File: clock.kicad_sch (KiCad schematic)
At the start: 8 parts, among them U17 74HC74, U9 74HCU04, Y1 3.58Mhz

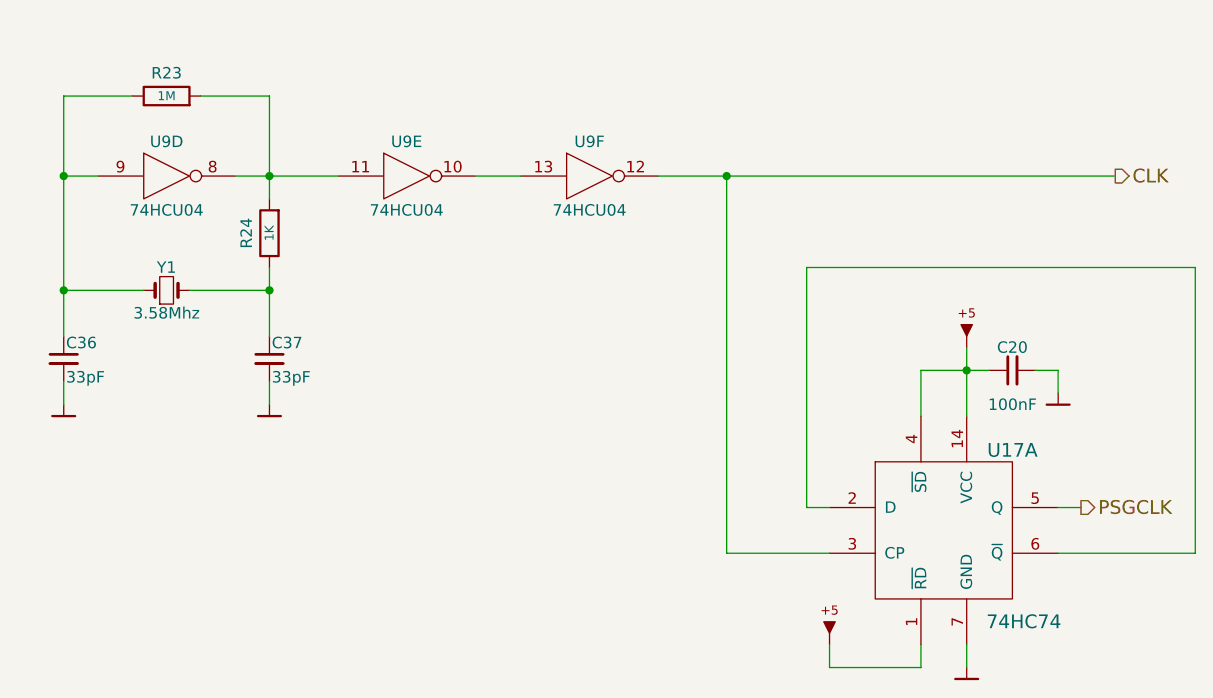
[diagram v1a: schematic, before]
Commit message: Use clock generator IC instead of oscillator
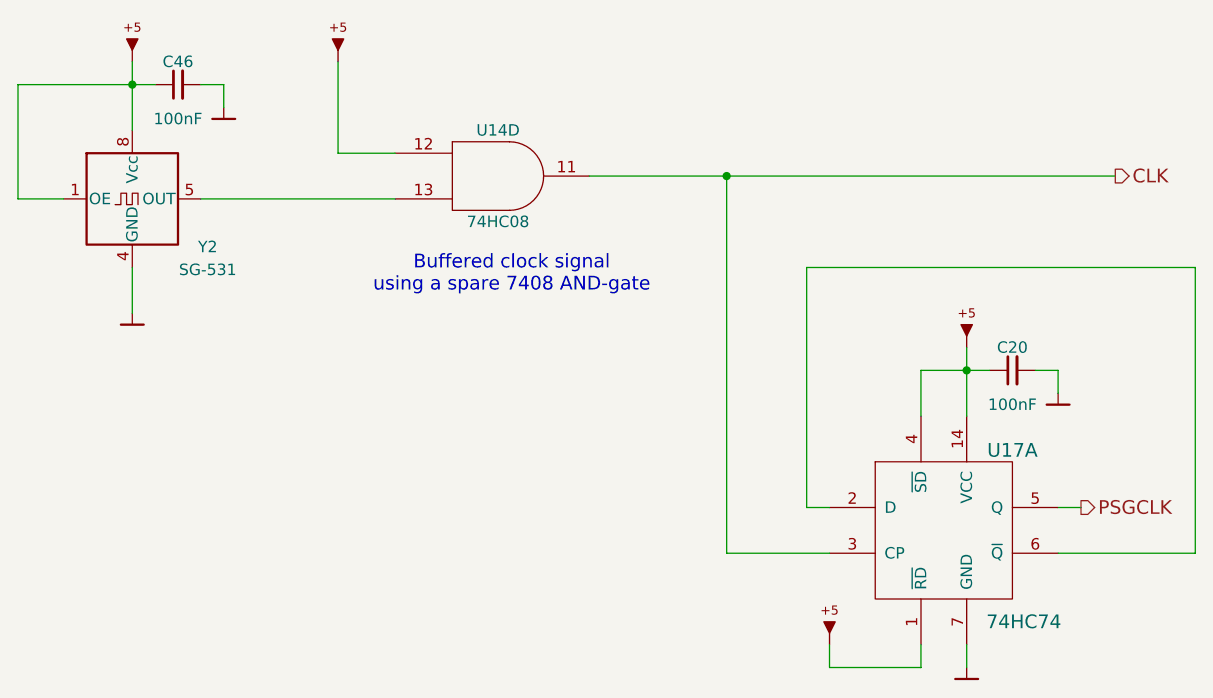
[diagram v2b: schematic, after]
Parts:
- removed C36, C37: 33pF, PCM_artemisa:Disc_capacitor, symbol PCM_artemisa:Cap
- removed R23: 1M, PCM_artemisa:Axial_resistor, symbol PCM_artemisa:R
- removed R24: 1K, PCM_artemisa:Axial_resistor, symbol PCM_artemisa:R
- removed U9: 74HCU04, PCM_artemisa:DIP-14_300, symbol PCM_artemisa:74HCU04
- removed Y1: 3.58Mhz, PCM_artemisa:Crystal, symbol PCM_artemisa:Crystal
- added C46: 100nF, PCM_artemisa:Disc_capacitor, symbol PCM_artemisa:Cap
- added U14: 74HC08, PCM_artemisa:DIP-14_300, symbol PCM_artemisa:74HC08
- added Y2: SG-531, Oscillator:Oscillator_SeikoEpson_SG-8002DC, symbol PCM_artemisa:SG-531
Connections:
- net CLK: now also U14.11
- net GND: now also C46.2, Y2.4 (GND)
- net VCC: now also C46.1, U14.12, Y2.1 (OE), Y2.8 (Vcc)
- new net: U14.13, Y2.5 (OUT)
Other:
- note added: "Buffered clock signal using a spare 7408 AND-gate"

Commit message: Re-annotate the whole schematic
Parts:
- renumbered C46 to C19, U14 to U6, U17 to U8, Y2 to Y1
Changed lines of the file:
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@@
 		(in_pos_files yes)
 		(dnp no)
-		(property "Reference" "U17"
+		(property "Reference" "U8"
 			(at 179.07 105.41 0)
 			(show_name no)
@@
 			(project "motherboard-hk10"
 				(path "/e63e39d7-6ac0-4ffd-8aa3-1841a4541b55/00000000-0000-0000-0000-00005bf74a85"
-					(reference "U17")
+					(reference "U8")
 					(unit 1)
 				)
@@
 		(in_pos_files yes)
 		(dnp no)
-		(property "Reference" "#PWR0127"
+		(property "Reference" "#PWR073"
 			(at 173.99 95.25 0)
 			(hide yes)
@@
 			(project "motherboard-hk10"
 				(path "/e63e39d7-6ac0-4ffd-8aa3-1841a4541b55/00000000-0000-0000-0000-00005bf74a85"
-					(reference "#PWR0127")
+					(reference "#PWR073")
 					(unit 1)
 				)
@@
 		(in_pos_files yes)
 		(dnp no)
-		(property "Reference" "#PWR0130"
+		(property "Reference" "#PWR072"
 			(at 158.75 128.27 0)
 			(hide yes)
@@
 			(project "motherboard-hk10"
 				(path "/e63e39d7-6ac0-4ffd-8aa3-1841a4541b55/00000000-0000-0000-0000-00005bf74a85"
-					(reference "#PWR0130")
+					(reference "#PWR072")
 					(unit 1)
 				)
@@
 		(in_pos_files yes)
 		(dnp no)
-		(property "Reference" "#PWR0163"
+		(property "Reference" "#PWR075"
 			(at 184.15 101.6 0)
 			(hide yes)
@@
 			(project "motherboard-hk10"
 				(path "/e63e39d7-6ac0-4ffd-8aa3-1841a4541b55/00000000-0000-0000-0000-00005bf74a85"
-					(reference "#PWR0163")
+					(reference "#PWR075")
 					(unit 1)
 				)
@@
 		(in_pos_files yes)
 		(dnp no)
-		(property "Reference" "#PWR0179"
+		(property "Reference" "#PWR074"
 			(at 173.99 132.08 0)
 			(hide yes)
@@
 			(project "motherboard-hk10"
 				(path "/e63e39d7-6ac0-4ffd-8aa3-1841a4541b55/00000000-0000-0000-0000-00005bf74a85"
-					(reference "#PWR0179")
+					(reference "#PWR074")
 					(unit 1)
 				)
@@
 		(in_pos_files yes)
 		(dnp no)
-		(property "Reference" "Y2"
+		(property "Reference" "Y1"
 			(at 89.662 82.804 0)
 			(show_name no)
@@
 			(project "motherboard-hk10"
 				(path "/e63e39d7-6ac0-4ffd-8aa3-1841a4541b55/00000000-0000-0000-0000-00005bf74a85"
-					(reference "Y2")
+					(reference "Y1")
 					(unit 1)
 				)
@@
 		(in_pos_files yes)
 		(dnp no)
-		(property "Reference" "#PWR0166"
+		(property "Reference" "#PWR070"
 			(at 91.44 69.85 0)
 			(hide yes)
@@
 			(project "motherboard-hk10"
 				(path "/e63e39d7-6ac0-4ffd-8aa3-1841a4541b55/00000000-0000-0000-0000-00005bf74a85"
-					(reference "#PWR0166")
+					(reference "#PWR070")
 					(unit 1)
 				)
@@
 		(in_pos_files yes)
 		(dnp no)
-		(property "Reference" "U14"
+		(property "Reference" "U6"
 			(at 121.92 69.85 0)
 			(show_name no)
@@
 			(project "motherboard-hk10"
 				(path "/e63e39d7-6ac0-4ffd-8aa3-1841a4541b55/00000000-0000-0000-0000-00005bf74a85"
-					(reference "U14")
+					(reference "U6")
 					(unit 4)
 				)
@@
 		(in_pos_files yes)
 		(dnp no)
-		(property "Reference" "C46"
+		(property "Reference" "C19"
 			(at 86.36 62.23 90)
 			(show_name no)
@@
 			(project "motherboard-hk10"
 				(path "/e63e39d7-6ac0-4ffd-8aa3-1841a4541b55/00000000-0000-0000-0000-00005bf74a85"
-					(reference "C46")
+					(reference "C19")
 					(unit 1)
 				)
@@
 		(in_pos_files yes)
 		(dnp no)
-		(property "Reference" "#PWR0128"
+		(property "Reference" "#PWR071"
 			(at 104.14 63.5 0)
 			(hide yes)
@@
 			(project "motherboard-hk10"
 				(path "/e63e39d7-6ac0-4ffd-8aa3-1841a4541b55/00000000-0000-0000-0000-00005bf74a85"
-					(reference "#PWR0128")
+					(reference "#PWR071")
 					(unit 1)
 				)
@@
 		(in_pos_files yes)
 		(dnp no)
-		(property "Reference" "#PWR0167"
+		(property "Reference" "#PWR069"
 			(at 81.28 92.71 0)
 			(hide yes)
@@
 			(project "motherboard-hk10"
 				(path "/e63e39d7-6ac0-4ffd-8aa3-1841a4541b55/00000000-0000-0000-0000-00005bf74a85"
-					(reference "#PWR0167")
+					(reference "#PWR069")
 					(unit 1)
 				)
@@
 		(in_pos_files yes)
 		(dnp no)
-		(property "Reference" "#PWR0148"
+		(property "Reference" "#PWR068"
 			(at 81.28 63.5 0)
 			(hide yes)
@@
 			(project "motherboard-hk10"
 				(path "/e63e39d7-6ac0-4ffd-8aa3-1841a4541b55/00000000-0000-0000-0000-00005bf74a85"
-					(reference "#PWR0148")
-					(unit 1)
-				)
+					(reference "#PWR068")
+					(unit 1)
+				)

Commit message: Resolve power connector pinout
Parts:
- Y1: footprint Oscillator:Oscillator_SeikoEpson_SG-8002DC -> PCM_artemisa:SG-531
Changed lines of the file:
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@@
 			)
 		)
-		(property "Footprint" "Oscillator:Oscillator_SeikoEpson_SG-8002DC"
+		(property "Footprint" "PCM_artemisa:SG-531"
 			(at 92.71 86.36 0)
 			(hide yes)

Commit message: Adjust footprints and draft PCB layout
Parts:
- C19, C20: footprint PCM_artemisa:Disc_capacitor -> Capacitor_THT:C_Disc_D5.0mm_W2.5mm_P2.50mm
- U6, U8: footprint PCM_artemisa:DIP-14_300 -> Package_DIP:DIP-14_W7.62mm
- Y1: footprint PCM_artemisa:SG-531 -> Oscillator:Oscillator_SeikoEpson_SG-8002DC
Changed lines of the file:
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@@
 			)
 		)
-		(property "Footprint" "PCM_artemisa:DIP-14_300"
+		(property "Footprint" "Package_DIP:DIP-14_W7.62mm"
 			(at 171.45 119.38 0)
 			(hide yes)
@@
 			)
 		)
-		(property "Footprint" "PCM_artemisa:Disc_capacitor"
+		(property "Footprint" "Capacitor_THT:C_Disc_D5.0mm_W2.5mm_P2.50mm"
 			(at 179.07 96.52 0)
 			(hide yes)
@@
 			)
 		)
-		(property "Footprint" "PCM_artemisa:SG-531"
+		(property "Footprint" "Oscillator:Oscillator_SeikoEpson_SG-8002DC"
 			(at 92.71 86.36 0)
 			(hide yes)
@@
 			)
 		)
-		(property "Footprint" "PCM_artemisa:DIP-14_300"
+		(property "Footprint" "Package_DIP:DIP-14_W7.62mm"
 			(at 111.76 73.025 0)
 			(hide yes)
@@
 			)
 		)
-		(property "Footprint" "PCM_artemisa:Disc_capacitor"
+		(property "Footprint" "Capacitor_THT:C_Disc_D5.0mm_W2.5mm_P2.50mm"
 			(at 86.36 64.77 0)
 			(hide yes)
